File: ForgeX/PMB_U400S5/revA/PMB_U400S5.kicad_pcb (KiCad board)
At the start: 2 copper layers, 197.5 x 49.3 mm, 26 parts, among them J1 Screw_Terminal_01x03, J10 Screw_Terminal_01x01, J11 Screw_Terminal_01x01, J12 Screw_Terminal_01x03, J13 Screw_Terminal_01x01, J14 Screw_Terminal_01x01, J15 Screw_Terminal_01x01, J16 Screw_Terminal_01x01, J17 Screw_Terminal_01x01, J18 Screw_Terminal_01x01, J2 Screw_Terminal_01x03, J3 Screw_Terminal_01x03, J4 Screw_Terminal_01x01, J5 Screw_Terminal_01x01, J6 Screw_Terminal_01x01, J7 Screw_Terminal_01x03, J8 Screw_Terminal_01x01, J9 Screw_Terminal_01x01

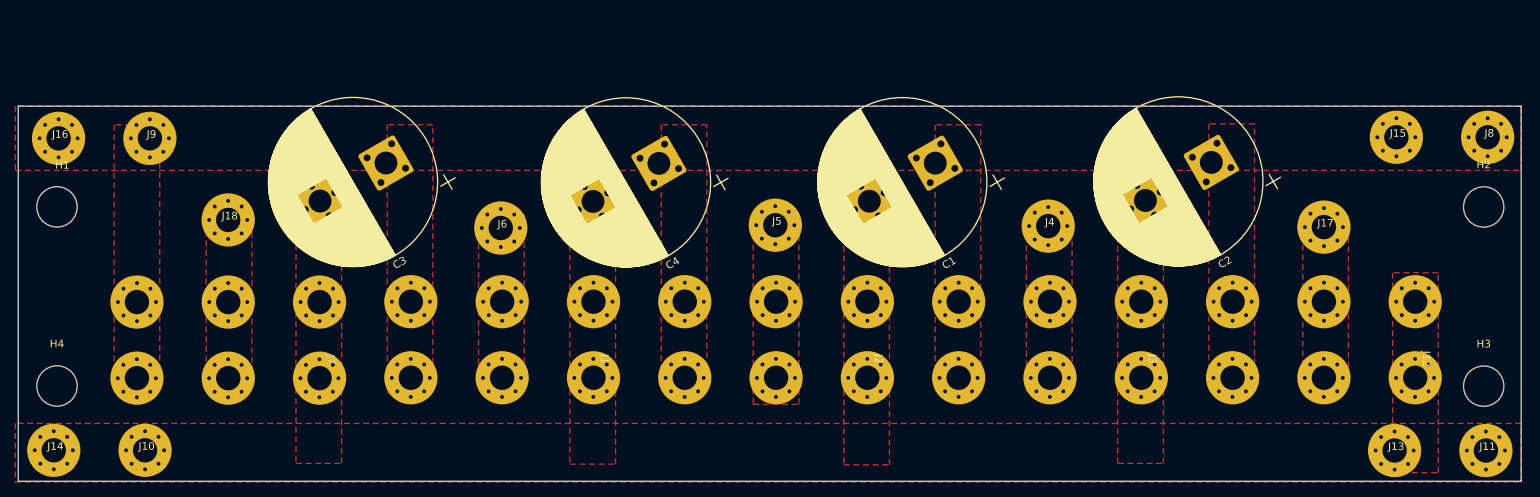
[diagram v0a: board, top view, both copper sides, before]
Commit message: Major redesign & Reworks
* Star grounding scheme enforced across the whole ForgeX design....
* Viper26 based PSU designed
* Better signal integrity & decoupling on LVP and major reroute
* Laminated DC bus (Biplanar) , instead of (Coplanar) , for heavily reduced bus inductance & equivelant Electrolytics ESL
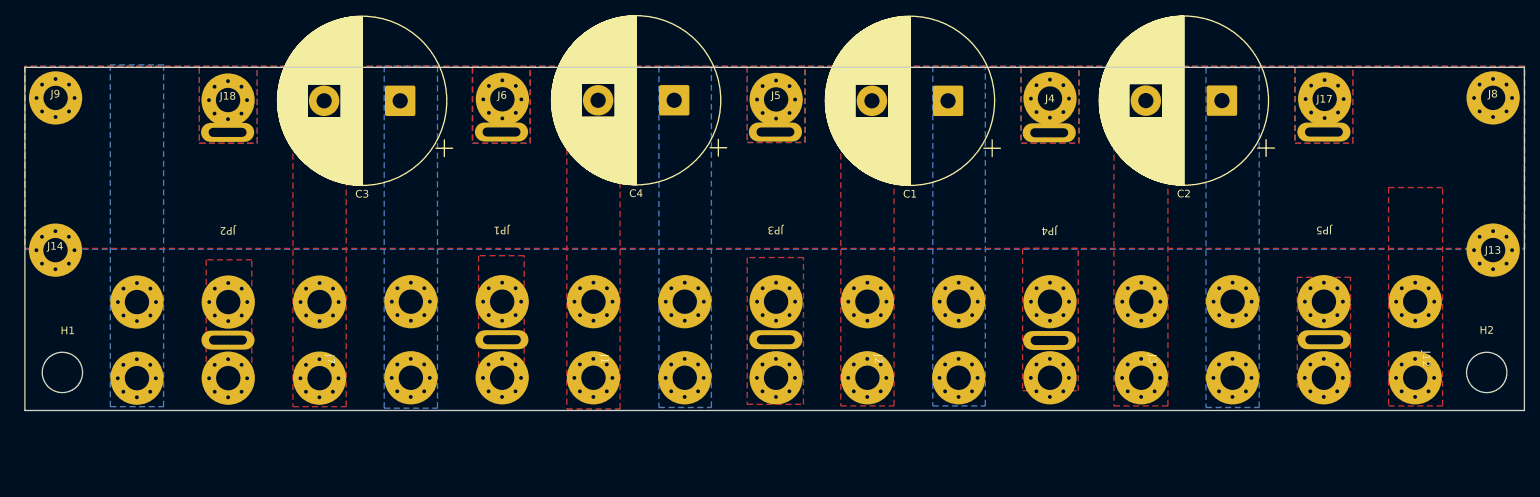
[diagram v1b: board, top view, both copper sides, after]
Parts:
- removed H3, H4: MountingHole, MountingHole:MountingHole_5.3mm_M5_DIN965
- removed J10, J11, J15, J16: Screw_Terminal_01x01, Libmain:M3_PCONN_1x01
- added JP1: Jumper_2_Bridged, Libmain:PowerJumper_PMB, F.Cu at (111.9, 59.1)
- added JP2: Jumper_2_Bridged, Libmain:PowerJumper_PMB, F.Cu at (75.9, 59.2)
- added JP3: Jumper_2_Bridged, Libmain:PowerJumper_PMB, F.Cu at (147.9, 59.1)
- added JP4: Jumper_2_Bridged, Libmain:PowerJumper_PMB, F.Cu at (183.9, 59.2)
- added JP5: Jumper_2_Bridged, Libmain:PowerJumper_PMB, F.Cu at (220.0, 59.1)
- C1, C2, C3, C4: footprint Libmain:CP_Radial_D22.0mm_P10.00mm_SnapIn_Ceye -> Capacitor_THT:CP_Radial_D22.0mm_P10.00mm_SnapIn
- moved J13 29.2 mm to (242.2, 62.2)
- moved J14 26.3 mm to (53.3, 62.2)
- moved H1 21.8 mm to (54.2, 78.3)
- moved H2 21.8 mm to (241.4, 78.3)
- moved J6 16.9 mm to (112.0, 42.4)
- moved J17 16.8 mm to (220.1, 42.3)
- moved J4 16.8 mm to (184.0, 42.3)
- moved J5 16.5 mm to (148.0, 42.4)
- moved J18 15.7 mm to (75.9, 42.5)
- moved J9 13.7 mm to (53.3, 42.2)
- moved C4 8.53 mm to (134.6, 42.5), turned to 180 degrees
- moved C3 8.39 mm to (98.6, 42.6), turned to 180 degrees
- moved C1 8.37 mm to (170.6, 42.6), turned to 180 degrees
- moved C2 8.24 mm to (206.6, 42.6), turned to 180 degrees
- moved J8 5.19 mm to (242.2, 42.2)
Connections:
- J17 pad 1: Net-(J12-Pin_2) -> Net-(J17-Pin_1)
- J4 pad 1: /Phase_{C} -> Net-(J4-Pin_1)
- J5 pad 1: /Phase_{B} -> Net-(J5-Pin_1)
- J6 pad 1: /Phase_{A} -> Net-(J6-Pin_1)
- J7 pad 2: Net-(J18-Pin_1) -> Net-(J7-Pin_2)
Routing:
- added copper zone on B.Cu, net HVDC
- added copper zone on B.Cu, net Net-(J17-Pin_1)
- added copper zone on F.Cu, net Net-(J17-Pin_1)
- added copper zone on B.Cu, net Net-(J18-Pin_1)
- added copper zone on B.Cu, net Net-(J4-Pin_1)
- added copper zone on F.Cu, net Net-(J4-Pin_1)
- added copper zone on B.Cu, net Net-(J5-Pin_1)
- added copper zone on F.Cu, net Net-(J5-Pin_1)
- added copper zone on B.Cu, net Net-(J6-Pin_1)
- added copper zone on F.Cu, net Net-(J6-Pin_1)
- added copper zone on F.Cu, net Net-(J7-Pin_2)
- removed copper zone on F.Cu, net HVDC
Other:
- board size 197.5 x 49.3 mm -> 197.1 x 45.1 mm
